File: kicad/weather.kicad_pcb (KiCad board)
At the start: 2 copper layers, 91.4 x 66 mm, 19 parts, among them J1 Barrel_Jack, Q1 2N7000, U1 BME680

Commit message: 4060
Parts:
- added C4: 1n, Capacitor_SMD:C_1206_3216Metric_Pad1.33x1.80mm_HandSolder, F.Cu at (18.4, 81.9)
- added C5: C, Capacitor_SMD:C_1206_3216Metric_Pad1.33x1.80mm_HandSolder, F.Cu at (24.9, 76.1)
- added Q2: 2N7000, Package_TO_SOT_THT:TO-92_Inline, F.Cu at (17.4, 77.7)
- added R5: 100k, Resistor_SMD:R_1206_3216Metric_Pad1.30x1.75mm_HandSolder, F.Cu at (18.4, 85.2)
- added R6: 1M, Resistor_SMD:R_1206_3216Metric_Pad1.30x1.75mm_HandSolder, F.Cu at (24.4, 81.9)
- added R7: R_US, Resistor_SMD:R_1206_3216Metric_Pad1.30x1.75mm_HandSolder, F.Cu at (30.9, 76.1)
- added R8: R_US, Resistor_SMD:R_1206_3216Metric_Pad1.30x1.75mm_HandSolder, F.Cu at (24.3, 85.2)
- added R9: R_US, Resistor_SMD:R_1206_3216Metric_Pad1.30x1.75mm_HandSolder, F.Cu at (30.3, 79.4)
- added U2: CD4060BM96, Package_SO:SOIC-16_3.9x9.9mm_P1.27mm, F.Cu at (18.4, 64.1)
- U1: value BME680 -> BME280
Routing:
- net Net-(A1-Pad6): track 32.9 -> 0.00 mm
- net Net-(D2-Pad1): track 17.6 -> 0.00 mm

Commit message: revisionB
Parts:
- Q1, Q2: footprint Package_TO_SOT_THT:TO-92_Inline -> Package_TO_SOT_SMD:SOT-23_Handsoldering
- moved Q2 64.7 mm to (76.2, 50.8), turned to 90 degrees
- moved R5 59.3 mm to (76.2, 72.4), turned to 180 degrees
- moved R8 59.0 mm to (76.2, 57.1), turned to 180 degrees
- moved C4 58.1 mm to (76.2, 76.2)
- moved R7 55.8 mm to (80.6, 50.8), turned to 90 degrees
- moved R6 53.5 mm to (76.2, 68.6), turned to 180 degrees
- moved C5 53.5 mm to (76.2, 61.0)
- moved U2 49.5 mm to (67.9, 65.4)
- moved R9 48.2 mm to (76.2, 64.8)
- moved R3 20.6 mm to (94.6, 78.7)
- moved C1 16.5 mm to (58.4, 59.7)
- moved R4 14.5 mm to (88.9, 76.2)
- moved R1 13.7 mm to (101.6, 78.7)
- moved R2 13.7 mm to (101.6, 83.8)
- moved Q1 1.90 mm to (127.0, 60.3), turned to 0 degrees
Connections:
- Q1 pad 1: GND -> Net-(A1-Pad6)
- Q1 pad 2: Net-(A1-Pad6) -> GND
- Q2 pad 1: GND -> Net-(Q2-Pad1)
- Q2 pad 2: Net-(Q2-Pad2) -> GND
- R8 pad 1: Net-(Q2-Pad2) -> Net-(Q2-Pad1)
- U2 pad 3: Net-(Q2-Pad2) -> Net-(Q2-Pad1)
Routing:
- net +3V3: track 87.3 -> 134.5 mm
- net Net-(A1-Pad17): track 127.5 -> 87.6 mm
- net GND: track 39.9 -> 0.00 mm
- net Net-(A1-Pad6): track 0.00 -> 30.4 mm
- net Net-(A1-Pad1): track 13.8 -> 43.1 mm
- net Net-(Q2-Pad1): track 0.00 -> 22.5 mm
- net Net-(D2-Pad1): track 0.00 -> 22.4 mm
- net Net-(A1-Pad18): track 90.0 -> 73.3 mm
- net +5V: track 76.8 -> 90.8 mm
- net Net-(D1-Pad2): track 22.2 -> 8.55 mm
- net Net-(D2-Pad2): track 32.3 -> 18.6 mm
- net Net-(C5-Pad1): track 0.00 -> 12.4 mm
- net Net-(C4-Pad1): track 0.00 -> 8.10 mm
- net Net-(C4-Pad2): track 0.00 -> 7.63 mm
- net Net-(R5-Pad2): track 0.00 -> 6.72 mm
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- added copper zone on B.Cu, net GND
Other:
- board text added: "REVISION B APRIL 2021"
- board text removed: "REVISION 1.1.1 DECEMBER 2020"

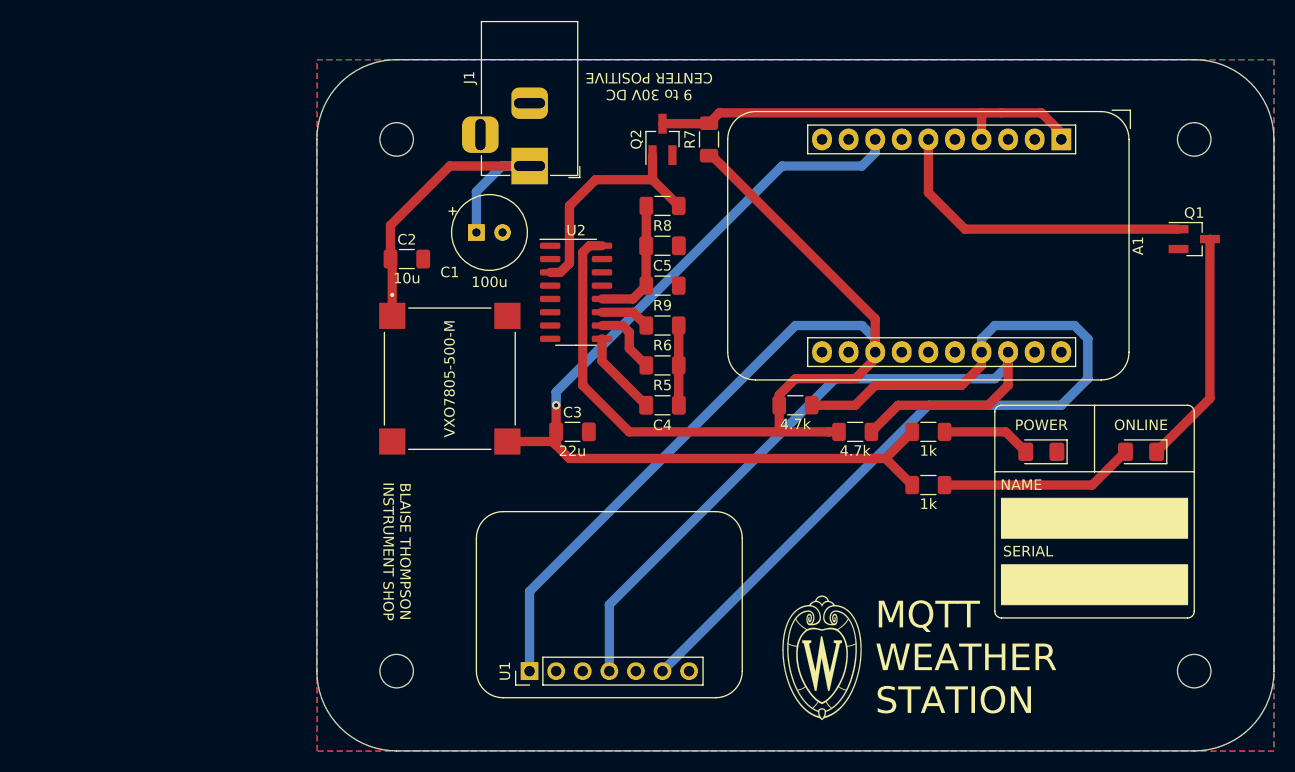
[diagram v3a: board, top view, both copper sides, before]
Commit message: C5 1u BOM
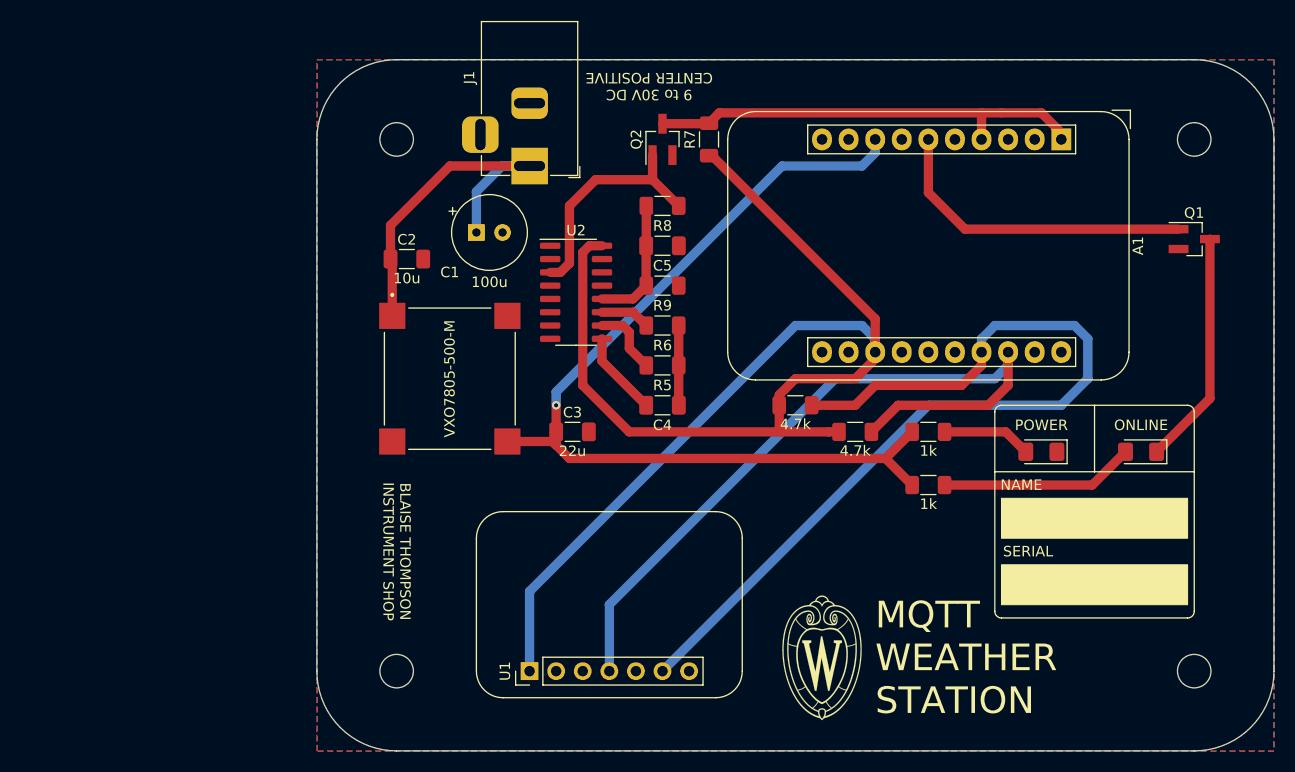
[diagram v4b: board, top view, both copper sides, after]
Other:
- net class Default removed
